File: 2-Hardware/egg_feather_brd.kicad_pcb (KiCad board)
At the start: 2 copper layers, 53.3 x 24.9 mm, 5 parts, among them SW1 SWITCH_SPST, U1 ADAFRUIT_FEATHER, U2 LIS3DH_BOB

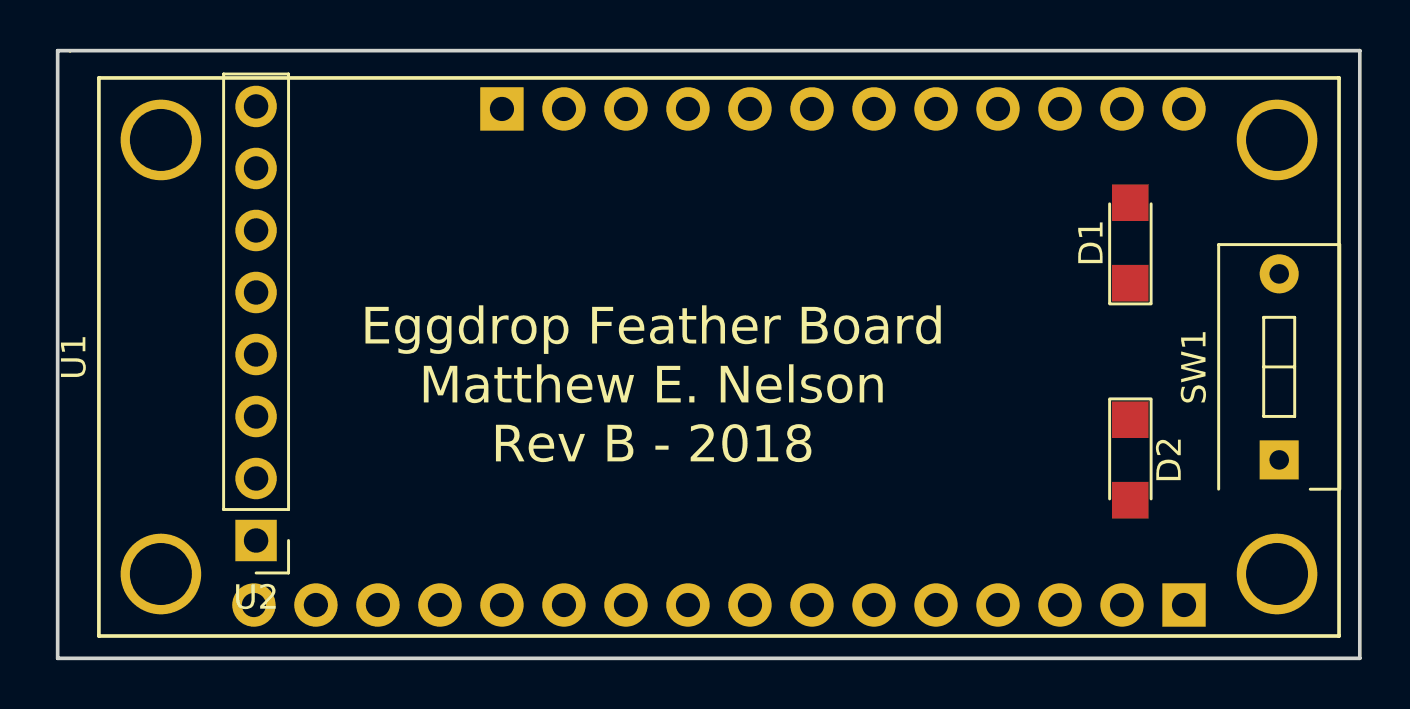
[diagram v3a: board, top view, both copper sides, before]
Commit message: Updates for KiCad 5, routed board for test run
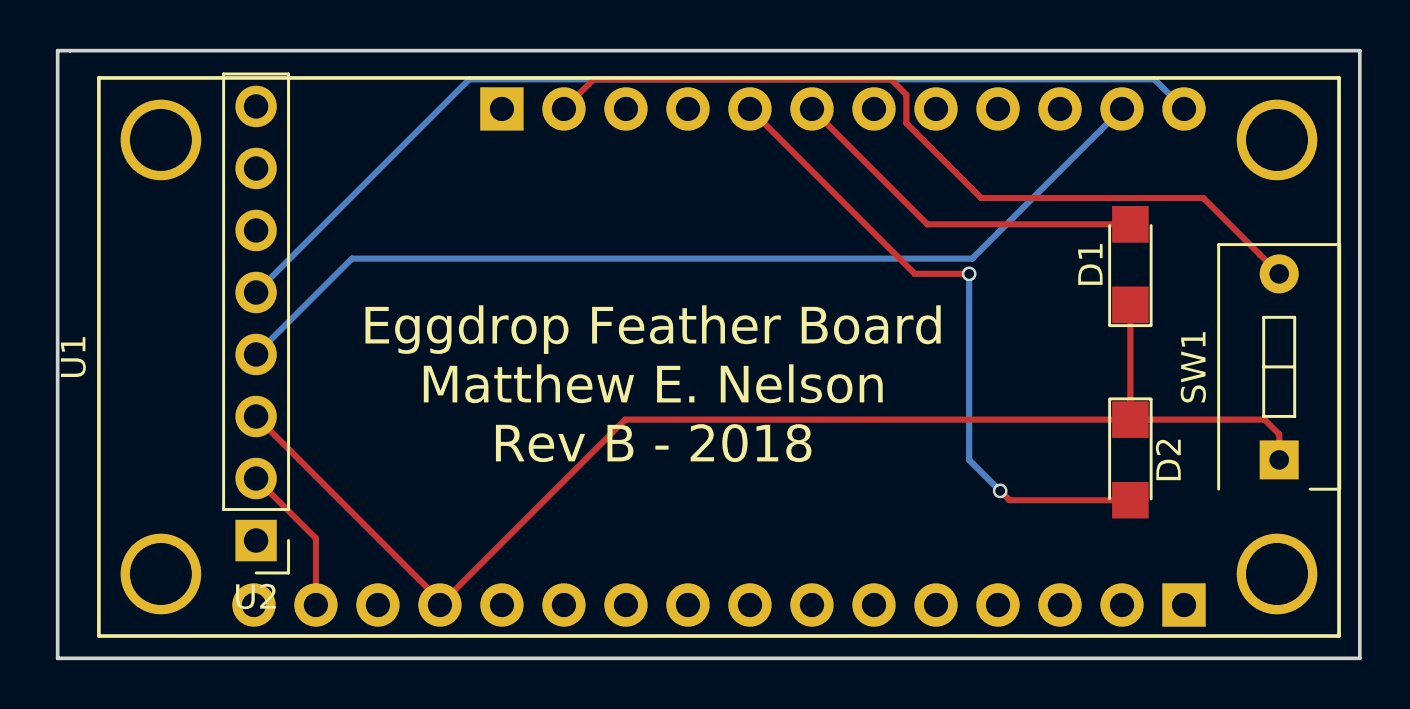
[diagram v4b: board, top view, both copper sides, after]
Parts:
- moved D1 0.89 mm to (165.4, 101.2)
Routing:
- net Net-(D1-Pad1): track 0.00 -> 54.4 mm
- net Net-(U1-Pad28): track 0.00 -> 42.1 mm
- net Net-(U1-Pad27): track 0.00 -> 39.6 mm
- net Net-(SW1-Pad2): track 0.00 -> 33.8 mm
- net Net-(D2-Pad2): track 0.00 -> 26.7 mm, vias 0 -> 2
- net Net-(D1-Pad2): track 0.00 -> 15.0 mm
- net Net-(U1-Pad15): track 0.00 -> 6.20 mm
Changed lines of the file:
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@@
-(kicad_pcb (version 4) (host pcbnew 4.0.7)
+(kicad_pcb (version 20171130) (host pcbnew "(5.0.0)")
   (general
-    (links 10)
-    (no_connects 10)
-    (area 121.336999 92.380999 174.827001 117.423001)
     (thickness 1.6)
     (drawings 6)
-    (tracks 0)
+    (tracks 36)
     (zones 0)
     (modules 5)
@@
       (layerselection 0x00030_80000001)
       (usegerberextensions false)
+      (usegerberattributes false)
+      (usegerberadvancedattributes false)
+      (creategerberjobfile false)
       (excludeedgelayer true)
       (linewidth 0.100000)
@@
       (hpglpennumber 1)
       (hpglpenspeed 20)
-      (hpglpendiameter 15)
-      (hpglpenoverlay 2)
+      (hpglpendiameter 15.000000)
       (psnegative false)
       (psa4output false)
@@
     (pad 8 thru_hole oval (at 0 17.78 180) (size 1.7 1.7) (drill 1) (layers *.Cu *.Mask))
     (model ${KISYS3DMOD}/Pin_Headers.3dshapes/Pin_Header_Straight_1x08_Pitch2.54mm.wrl
-      (at (xyz 0 -0.35 0))
+      (offset (xyz 0 -8.889999866485596 0))
       (scale (xyz 1 1 1))
       (rotate (xyz 0 0 90))
@@
   )
   (module LEDs:LED_1206 (layer F.Cu)
-    (at 165.354 100.33 90)
+    (at 165.354 101.22 90)
     (descr "LED 1206 smd package")
     (tags "LED led 1206 SMD smd SMT smt smdled SMDLED smtled SMTLED")
@@
     )
   )
+  (gr_text "Eggdrop Feather Board\nMatthew E. Nelson\nRev B - 2018" (at 145.796 106.172) (layer F.SilkS)
+    (effects (font (size 1.5 1.5) (thickness 0.3)))
+  )
   (gr_line (start 121.412 92.456) (end 121.92 92.456) (angle 90) (layer Edge.Cuts) (width 0.15))
   (gr_line (start 121.412 117.348) (end 121.412 92.456) (angle 90) (layer Edge.Cuts) (width 0.15))
@@
   (gr_line (start 174.752 92.456) (end 174.752 117.348) (angle 90) (layer Edge.Cuts) (width 0.15))
   (gr_line (start 121.92 92.456) (end 174.752 92.456) (angle 90) (layer Edge.Cuts) (width 0.15))
-  (gr_text "Eggdrop Feather Board\nMatthew E. Nelson\nRev B - 2018" (at 145.796 106.172) (layer F.SilkS)
-    (effects (font (size 1.5 1.5) (thickness 0.3)))
-  )
+  (segment (start 137.071 114.973) (end 137.071 115.164) (width 0.25) (layer F.Cu) (net 1))
+  (segment (start 129.54 107.442) (end 137.071 114.973) (width 0.25) (layer F.Cu) (net 1))
+  (segment (start 171.45 108.17) (end 171.45 109.22) (width 0.25) (layer F.Cu) (net 1))
+  (segment (start 170.85 107.57) (end 171.45 108.17) (width 0.25) (layer F.Cu) (net 1))
+  (segment (start 165.354 107.57) (end 170.85 107.57) (width 0.25) (layer F.Cu) (net 1))
+  (segment (start 165.354 102.87) (end 165.354 107.57) (width 0.25) (layer F.Cu) (net 1))
+  (segment (start 144.665 107.57) (end 165.354 107.57) (width 0.25) (layer F.Cu) (net 1))
+  (segment (start 137.071 115.164) (end 144.665 107.57) (width 0.25) (layer F.Cu) (net 1))
+  (segment (start 157.037 99.57) (end 165.354 99.57) (width 0.25) (layer F.Cu) (net 2))
+  (segment (start 152.311 94.844) (end 157.037 99.57) (width 0.25) (layer F.Cu) (net 2))
+  (via (at 158.75 101.6) (size 0.6) (drill 0.4) (layers F.Cu B.Cu) (net 3))
+  (segment (start 149.771 94.844) (end 156.527 101.6) (width 0.25) (layer F.Cu) (net 3))
+  (segment (start 156.527 101.6) (end 158.75 101.6) (width 0.25) (layer F.Cu) (net 3))
+  (via (at 160.02 110.49) (size 0.6) (drill 0.4) (layers F.Cu B.Cu) (net 3))
+  (segment (start 158.75 101.6) (end 158.75 109.22) (width 0.25) (layer B.Cu) (net 3))
+  (segment (start 158.75 109.22) (end 160.02 110.49) (width 0.25) (layer B.Cu) (net 3))
+  (segment (start 160.4 110.87) (end 165.354 110.87) (width 0.25) (layer F.Cu) (net 3))
+  (segment (start 160.02 110.49) (end 160.4 110.87) (width 0.25) (layer F.Cu) (net 3))
+  (segment (start 168.344999 98.494999) (end 170.650001 100.800001) (width 0.25) (layer F.Cu) (net 4))
+  (segment (start 159.245277 98.494999) (end 168.344999 98.494999) (width 0.25) (layer F.Cu) (net 4))
+  (segment (start 156.176999 95.426721) (end 159.245277 98.494999) (width 0.25) (layer F.Cu) (net 4))
+  (segment (start 155.545719 93.629999) (end 156.176999 94.261279) (width 0.25) (layer F.Cu) (net 4))
+  (segment (start 170.650001 100.800001) (end 171.45 101.6) (width 0.25) (layer F.Cu) (net 4))
+  (segment (start 156.176999 94.261279) (end 156.176999 95.426721) (width 0.25) (layer F.Cu) (net 4))
+  (segment (start 143.365001 93.629999) (end 155.545719 93.629999) (width 0.25) (layer F.Cu) (net 4))
+  (segment (start 142.151 94.844) (end 143.365001 93.629999) (width 0.25) (layer F.Cu) (net 4))
+  (segment (start 131.991 112.433) (end 131.991 115.164) (width 0.25) (layer F.Cu) (net 5))
+  (segment (start 129.54 109.982) (end 131.991 112.433) (width 0.25) (layer F.Cu) (net 5))
+  (segment (start 164.122001 95.732999) (end 165.011 94.844) (width 0.25) (layer B.Cu) (net 6))
+  (segment (start 158.880001 100.974999) (end 164.122001 95.732999) (width 0.25) (layer B.Cu) (net 6))
+  (segment (start 133.467001 100.974999) (end 158.880001 100.974999) (width 0.25) (layer B.Cu) (net 6))
+  (segment (start 129.54 104.902) (end 133.467001 100.974999) (width 0.25) (layer B.Cu) (net 6))
+  (segment (start 166.662001 93.955001) (end 167.551 94.844) (width 0.25) (layer B.Cu) (net 7))
+  (segment (start 166.336999 93.629999) (end 166.662001 93.955001) (width 0.25) (layer B.Cu) (net 7))
+  (segment (start 138.272001 93.629999) (end 166.336999 93.629999) (width 0.25) (layer B.Cu) (net 7))
+  (segment (start 129.54 102.362) (end 138.272001 93.629999) (width 0.25) (layer B.Cu) (net 7))
 )
